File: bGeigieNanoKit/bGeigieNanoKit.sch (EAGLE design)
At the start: 36 parts, among them T1 2SC1815

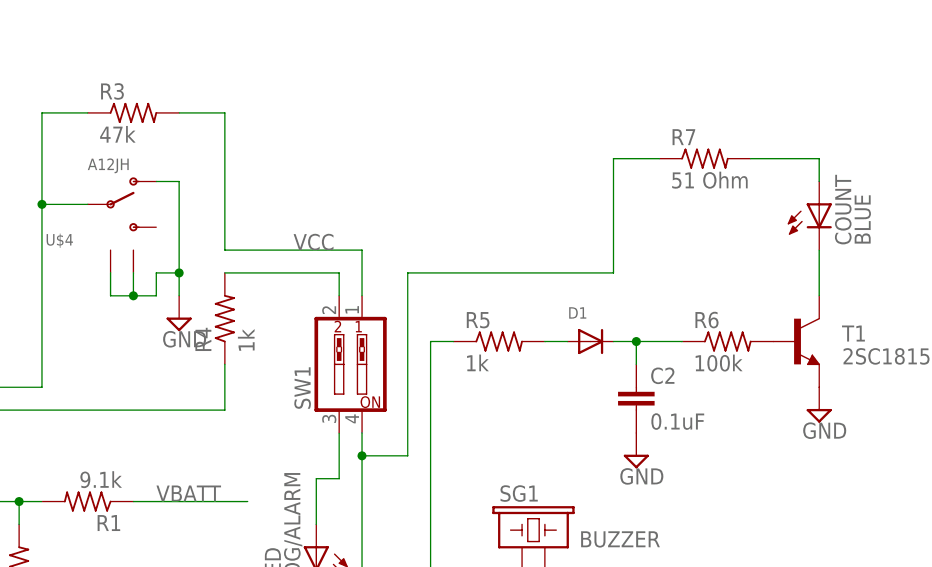
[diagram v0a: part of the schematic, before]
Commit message: Changed R8 to 47k and and R9 to 4.7k and fixed some overlaying text.
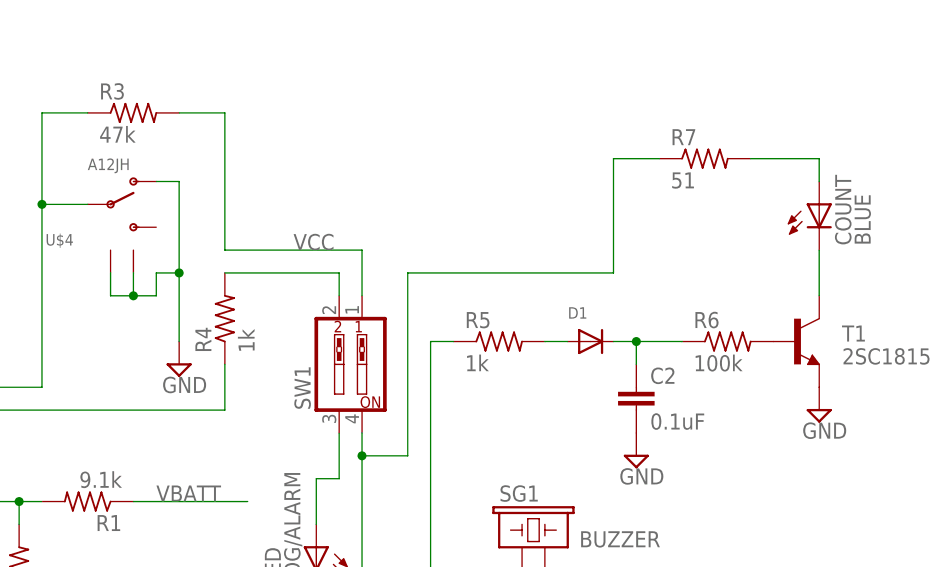
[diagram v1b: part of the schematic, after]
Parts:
- R7: value 51 Ohm -> 51
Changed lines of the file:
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@@
 <part name="R5" library="rcl" deviceset="R-US_" device="0207/10" value="1k"/>
 <part name="R6" library="rcl" deviceset="R-US_" device="0207/10" value="100k"/>
-<part name="R7" library="rcl" deviceset="R-US_" device="0207/10" value="51 Ohm"/>
+<part name="R7" library="rcl" deviceset="R-US_" device="0207/10" value="  51"/>
 <part name="R8" library="rcl" deviceset="R-US_" device="0207/10" value="47k"/>
 <part name="R9" library="rcl" deviceset="R-US_" device="0207/10" value="4.7k"/>
@@
 <instance part="SUPPLY8" gate="GND" x="101.6" y="60.96"/>
 <instance part="SUPPLY9" gate="GND" x="185.42" y="88.9"/>
-<instance part="SUPPLY10" gate="GND" x="170.18" y="124.46"/>
+<instance part="SUPPLY10" gate="GND" x="170.18" y="119.38"/>
 <instance part="R1" gate="G$1" x="160.02" y="104.14" rot="R180"/>
 <instance part="R2" gate="G$1" x="152.4" y="96.52" rot="R90"/>
@@
 <wire x1="167.64" y1="127" x2="167.64" y2="129.54" width="0.1524" layer="91"/>
 <pinref part="SUPPLY10" gate="GND" pin="GND"/>
-<wire x1="170.18" y1="127" x2="170.18" y2="129.54" width="0.1524" layer="91"/>
+<wire x1="170.18" y1="121.92" x2="170.18" y2="129.54" width="0.1524" layer="91"/>
 <wire x1="167.64" y1="129.54" x2="170.18" y2="129.54" width="0.1524" layer="91"/>
 <pinref part="U$4" gate="G$1" pin="GND@2"/>
